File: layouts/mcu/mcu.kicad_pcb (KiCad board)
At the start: 2 copper layers, 15 parts

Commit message: Layouts: mcu: place and route mcu, add jlc design rules
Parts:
- C3, C4: value 100nF ±10% 50V X7R -> 20pF ±5% 50V C0G; footprint atopile:C0603-bd72f6 -> atopile:C0402-b3ef17
- R3: value 10kΩ ±1% 100mW -> 0Ω 100mW
- moved R5 26.6 mm to (6.60, -2.40)
- moved S2 17.5 mm to (-5.43, 9.60), turned to -90 degrees
- moved S1 16.6 mm to (4.17, 9.60), turned to 90 degrees
- moved C3 13.5 mm to (9.95, 2.65), turned to -90 degrees
- moved C2 13.1 mm to (-2.40, 8.30), turned to -90 degrees
- moved R2 12.1 mm to (1.60, 8.20), turned to -90 degrees
- moved R4 11.8 mm to (-0.75, 8.20), turned to -90 degrees
- moved R3 11.3 mm to (6.50, 3.20), turned to -90 degrees
- moved R6 9.29 mm to (-3.00, 11.2), turned to 90 degrees
- moved XTAL1 9.13 mm to (8.30, 3.80), turned to -90 degrees
- moved C4 7.90 mm to (9.95, 4.95), turned to 90 degrees
- moved C5 7.72 mm to (-1.42, 11.2), turned to -90 degrees
- moved R1 2.10 mm to (1.75, 11.2)
- moved C1 1.48 mm to (0.17, 11.2)
- turned U1 to 90 degrees
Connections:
- C1 pad 1: mcu.boot_switch.lp_filter-line -> mcu-line-5
- C1 pad 2: mcu.boot_switch.lp_filter-gnd -> gnd
- C2 pad 2: mcu-gnd -> gnd
- C3 pad 2: mcu-gnd -> gnd
- C4 pad 1: mcu-line-4 -> mcu-line-9
- C4 pad 2: mcu-gnd -> gnd
- C5 pad 1: mcu.reset_switch.lp_filter-line -> mcu-line-3
- C5 pad 2: mcu.reset_switch.lp_filter-gnd -> gnd
- R1 pad 2: mcu.boot_switch.lp_filter-line -> mcu-line-5
- R2 pad 1: mcu-line -> mcu-line-5
- R3 pad 2: mcu-line-1 -> mcu-line
- R4 pad 1: mcu-line-7 -> mcu-line-2
- R5 pad 1: mcu-line-9 -> mcu-line-4
- R6 pad 2: mcu.reset_switch.lp_filter-line -> mcu-line-3
- S1 pad 3: mcu-gnd -> gnd
- S1 pad 4: mcu-gnd -> gnd
- S2 pad 3: mcu-gnd -> gnd
- S2 pad 4: mcu-gnd -> gnd
- U1 pad 1: mcu-gnd -> gnd
- U1 pad 11: mcu-gnd -> gnd
- U1 pad 12: mcu-line-4 -> mcu-line-9
- U1 pad 13: mcu-line-1 -> mcu-line
- U1 pad 14: mcu-gnd -> gnd
- U1 pad 16: mcu.esp32_c3_mini_1.ic-line-5 -> mcu.esp32_c3_mini_1.ic-line-4
- U1 pad 18: mcu.esp32_c3_mini_1.ic-line-4 -> mcu.esp32_c3_mini_1.ic-line-5
- U1 pad 19: mcu.esp32_c3_mini_1.ic-line -> mcu.esp32_c3_mini_1.ic-line-3
- U1 pad 2: mcu-gnd -> gnd
- U1 pad 20: mcu.esp32_c3_mini_1.ic-line-3 -> mcu.esp32_c3_mini_1.ic-line-2
- U1 pad 21: mcu.esp32_c3_mini_1.ic-line-2 -> mcu.esp32_c3_mini_1.ic-line
- U1 pad 22: mcu-line-9 -> mcu-line-4
- U1 pad 23: mcu-line-8 -> mcu-line-3
- U1 pad 26: mcu-line-5 -> mcu-line-1
- U1 pad 27: mcu-line-3 -> mcu-line-6
- U1 pad 30: mcu-line-2 -> mcu-line-7
- U1 pad 31: mcu-line-6 -> mcu-line-8
- U1 pad 36: mcu-gnd -> gnd
- U1 pad 37: mcu-gnd -> gnd
- U1 pad 38: mcu-gnd -> gnd
- U1 pad 39: mcu-gnd -> gnd
- U1 pad 40: mcu-gnd -> gnd
- U1 pad 41: mcu-gnd -> gnd
- U1 pad 42: mcu-gnd -> gnd
- U1 pad 43: mcu-gnd -> gnd
- U1 pad 44: mcu-gnd -> gnd
- U1 pad 45: mcu-gnd -> gnd
- U1 pad 46: mcu-gnd -> gnd
- U1 pad 47: mcu-gnd -> gnd
- U1 pad 48: mcu-gnd -> gnd
- U1 pad 49: mcu-gnd -> gnd
- U1 pad 5: mcu-line-7 -> mcu-line-2
- U1 pad 50: mcu-gnd -> gnd
- U1 pad 51: mcu-gnd -> gnd
- U1 pad 52: mcu-gnd -> gnd
- U1 pad 53: mcu-gnd -> gnd
- U1 pad 54: mcu-gnd -> gnd
- U1 pad 55: mcu-gnd -> gnd
- U1 pad 56: mcu-gnd -> gnd
- U1 pad 57: mcu-gnd -> gnd
- U1 pad 58: mcu-gnd -> gnd
- U1 pad 59: mcu-gnd -> gnd
- U1 pad 60: mcu-gnd -> gnd
- U1 pad 61: mcu-gnd -> gnd
- U1 pad 8: mcu-line -> mcu-line-5
- XTAL1 pad 2: mcu-line-4 -> mcu-line-9
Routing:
- net mcu-line-3: track 0.00 -> 22.1 mm, vias 0 -> 2
- net mcu-gnd: track 10.9 -> 0.00 mm
- net hv: track 0.00 -> 7.66 mm, vias 0 -> 3
- net mcu-line-5: track 0.00 -> 7.37 mm
- net mcu.reset_switch-line: track 0.00 -> 5.64 mm
- net mcu.boot_switch-line: track 0.00 -> 5.63 mm
- net mcu-line-9: track 0.00 -> 5.28 mm
- net mcu.low_speed_crystal_clock-net: track 1.81 -> 3.66 mm
- net mcu-line: track 0.00 -> 1.57 mm
- net gnd: vias 0 -> 39
- added copper zone on F.Cu, net gnd

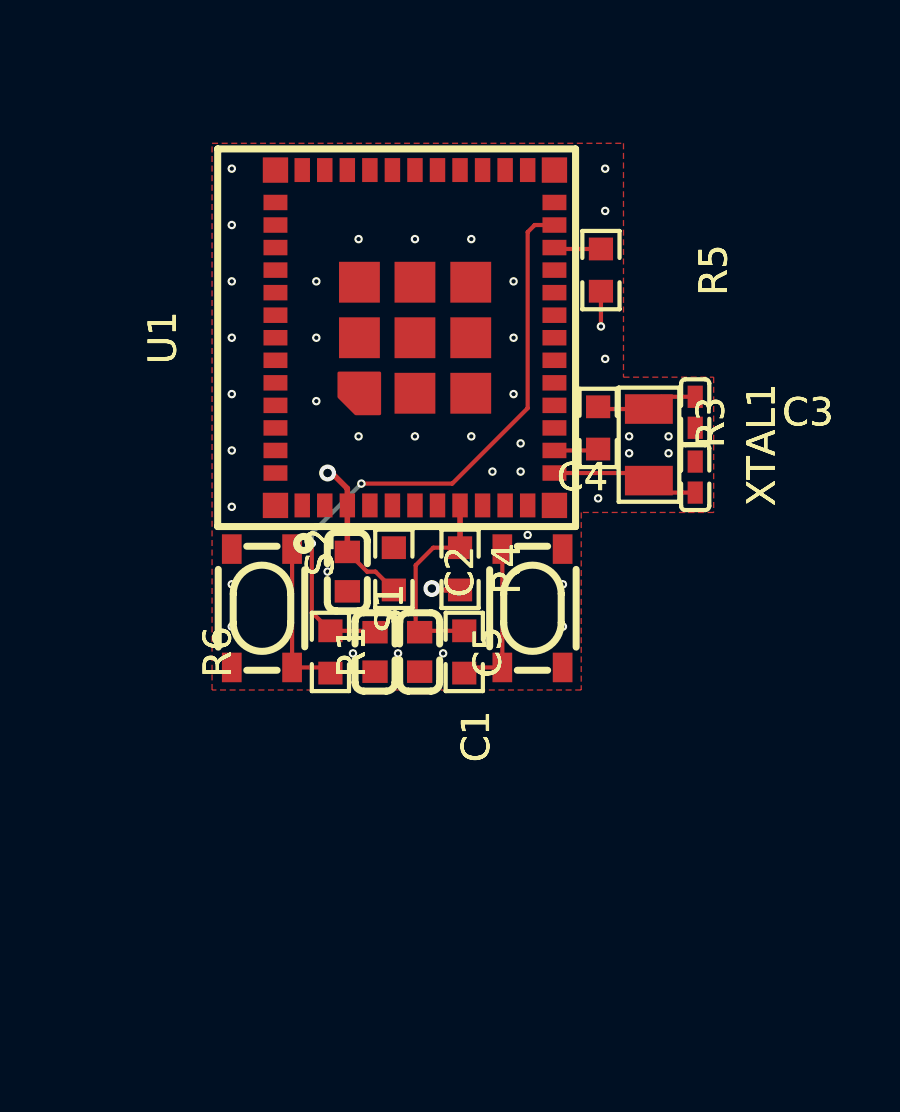
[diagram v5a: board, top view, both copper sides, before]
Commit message: Layouts: place light sensor between LEDs, add rule areas
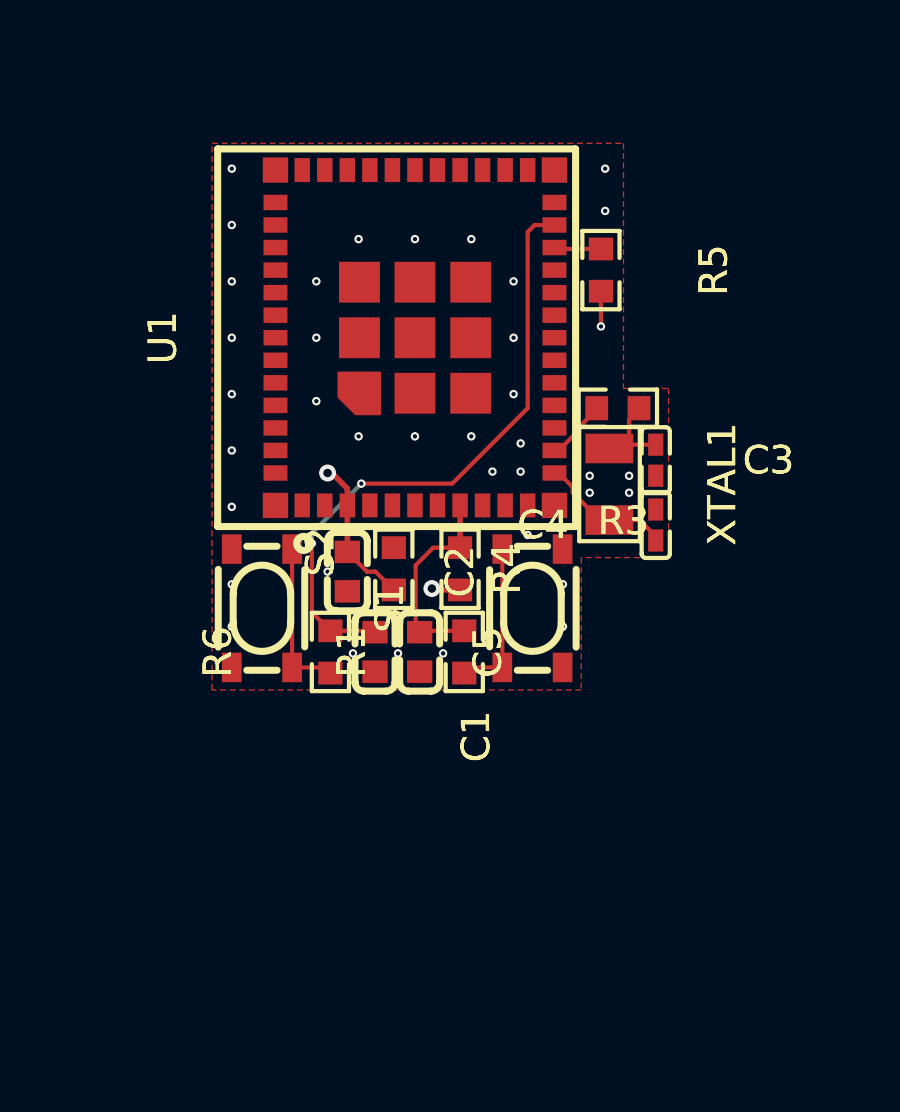
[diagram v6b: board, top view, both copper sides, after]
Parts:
- moved C3 2.20 mm to (8.54, 4.34)
- moved C4 2.20 mm to (8.54, 6.64)
- moved XTAL1 1.98 mm to (6.90, 5.20)
- moved R3 0.99 mm to (7.20, 2.50), turned to 180 degrees
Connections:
- C1 pad 1: mcu-line-5 -> mcu-line-1
- C4 pad 1: mcu-line-9 -> mcu-line
- C5 pad 1: mcu-line-3 -> mcu-line-6
- R1 pad 2: mcu-line-5 -> mcu-line-1
- R2 pad 1: mcu-line-5 -> mcu-line-1
- R3 pad 2: mcu-line -> mcu-line-4
- R5 pad 1: mcu-line-4 -> mcu-line-7
- R6 pad 2: mcu-line-3 -> mcu-line-6
- U1 pad 12: mcu-line-9 -> mcu-line
- U1 pad 13: mcu-line -> mcu-line-4
- U1 pad 16: mcu.esp32_c3_mini_1.ic-line-4 -> mcu.esp32_c3_mini_1.ic-line-2
- U1 pad 18: mcu.esp32_c3_mini_1.ic-line-5 -> mcu.esp32_c3_mini_1.ic-line-1
- U1 pad 19: mcu.esp32_c3_mini_1.ic-line-3 -> mcu.esp32_c3_mini_1.ic-line-5
- U1 pad 20: mcu.esp32_c3_mini_1.ic-line-2 -> mcu.esp32_c3_mini_1.ic-line-4
- U1 pad 22: mcu-line-4 -> mcu-line-7
- U1 pad 23: mcu-line-3 -> mcu-line-6
- U1 pad 26: mcu-line-1 -> mcu-line-8
- U1 pad 27: mcu-line-6 -> mcu-line-3
- U1 pad 30: mcu-line-7 -> mcu-line-9
- U1 pad 31: mcu-line-8 -> mcu-line-5
- U1 pad 6: mcu.esp32_c3_mini_1.ic-line-1 -> mcu.esp32_c3_mini_1.ic-line-3
- U1 pad 8: mcu-line-5 -> mcu-line-1
- XTAL1 pad 2: mcu-line-9 -> mcu-line
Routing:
- net mcu-line-6: track 0.00 -> 22.1 mm, vias 0 -> 2
- net mcu-line-3: track 22.1 -> 0.00 mm, vias 2 -> 0
- net mcu-line-5: track 7.37 -> 0.00 mm
- net mcu-line-1: track 0.00 -> 7.37 mm
- net mcu-line-9: track 5.28 -> 0.00 mm
- net mcu-line: track 1.57 -> 4.79 mm
- net mcu-line-7: track 0.00 -> 1.67 mm
- net mcu-line-4: track 1.67 -> 2.21 mm
- net gnd: vias 39 -> 37

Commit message: do some layouts
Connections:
- net mcu.low_speed_crystal_clock-net renamed unnamed[0]
- C1 pad 1: mcu-line-1 -> mcu-line
- C4 pad 1: mcu-line -> mcu-line-7
- C5 pad 1: mcu-line-6 -> mcu-line-2
- R1 pad 2: mcu-line-1 -> mcu-line
- R2 pad 1: mcu-line-1 -> mcu-line
- R4 pad 1: mcu-line-2 -> mcu-line-1
- R5 pad 1: mcu-line-7 -> mcu-line-9
- R6 pad 2: mcu-line-6 -> mcu-line-2
- U1 pad 12: mcu-line -> mcu-line-7
- U1 pad 16: mcu.esp32_c3_mini_1.ic-line-2 -> mcu.esp32_c3_mini_1.ic-line-3
- U1 pad 19: mcu.esp32_c3_mini_1.ic-line-5 -> mcu.esp32_c3_mini_1.ic-line-2
- U1 pad 21: mcu.esp32_c3_mini_1.ic-line -> mcu.esp32_c3_mini_1.ic-line-5
- U1 pad 22: mcu-line-7 -> mcu-line-9
- U1 pad 23: mcu-line-6 -> mcu-line-2
- U1 pad 26: mcu-line-8 -> mcu-line-5
- U1 pad 30: mcu-line-9 -> mcu-line-6
- U1 pad 31: mcu-line-5 -> mcu-line-8
- U1 pad 5: mcu-line-2 -> mcu-line-1
- U1 pad 6: mcu.esp32_c3_mini_1.ic-line-3 -> mcu.esp32_c3_mini_1.ic-line
- U1 pad 8: mcu-line-1 -> mcu-line
- XTAL1 pad 2: mcu-line -> mcu-line-7
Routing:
- net mcu-line-6: track 22.1 -> 0.00 mm, vias 2 -> 0
- net mcu-line-2: track 0.07 -> 22.1 mm, vias 0 -> 2
- net mcu-line-1: track 7.37 -> 0.07 mm
- net mcu-line-7: track 1.67 -> 4.79 mm
- net mcu-line: track 4.79 -> 7.37 mm
- net mcu-line-9: track 0.00 -> 1.67 mm
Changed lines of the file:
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@@
             (outputdirectory "")))
     (net 0 "")
-    (net 1 "mcu-line-8")
+    (net 1 "mcu-line-5")
     (net 2 "mcu.esp32_c3_mini_1.ic.footprint.pins[26].net-net")
-    (net 3 "mcu-line-9")
+    (net 3 "mcu-line-6")
     (net 4 "mcu.esp32_c3_mini_1.ic.footprint.pins[8].net-net")
     (net 5 "mcu.esp32_c3_mini_1.ic.footprint.pins[28].net-net")
-    (net 6 "mcu.esp32_c3_mini_1.ic-line-5")
+    (net 6 "mcu.esp32_c3_mini_1.ic-line-2")
     (net 7 "mcu.esp32_c3_mini_1.ic.footprint.pins[25].net-net")
-    (net 8 "mcu.esp32_c3_mini_1.ic-line-2")
+    (net 8 "mcu.esp32_c3_mini_1.ic-line-3")
     (net 9 "mcu-line-3")
     (net 10 "mcu.esp32_c3_mini_1.ic.footprint.pins[60].net-net")
-    (net 11 "mcu-line-7")
-    (net 12 "mcu.esp32_c3_mini_1.ic-line-3")
+    (net 11 "mcu-line-9")
+    (net 12 "mcu.esp32_c3_mini_1.ic-line")
     (net 13 "mcu.esp32_c3_mini_1.ic.footprint.pins[16].net-net")
-    (net 14 "mcu-line-2")
+    (net 14 "mcu-line-1")
     (net 15 "mcu.esp32_c3_mini_1.ic.footprint.pins[58].net-net")
     (net 16 "mcu.esp32_c3_mini_1.ic.footprint.pins[21].net-net")
     (net 17 "mcu.esp32_c3_mini_1.ic-line-1")
-    (net 18 "mcu.esp32_c3_mini_1.ic-line")
+    (net 18 "mcu.esp32_c3_mini_1.ic-line-5")
     (net 19 "hv")
-    (net 20 "mcu-line-5")
+    (net 20 "mcu-line-8")
     (net 21 "mcu.esp32_c3_mini_1.ic.footprint.pins[1].net-net")
     (net 22 "mcu-line-4")
@@
     (net 28 "mcu.esp32_c3_mini_1.ic.footprint.pins[17].net-net")
     (net 29 "mcu.esp32_c3_mini_1.ic.footprint.pins[27].net-net")
-    (net 30 "mcu-line")
+    (net 30 "mcu-line-7")
     (net 31 "mcu.boot_switch-line")
     (net 32 "mcu.reset_switch-line")
-    (net 33 "mcu.low_speed_crystal_clock-net")
-    (net 34 "mcu-line-1")
-    (net 35 "mcu-line-6")
+    (net 33 "unnamed[0]")
+    (net 34 "mcu-line")
+    (net 35 "mcu-line-2")
     (footprint "atopile:KEY-SMD_4P-L4.2-W3.2-P2.20-LS4.6-a2ccf0"
         (layer "F.Cu")
@@
             (layers "F.Cu" "F.Paste" "F.Mask")
             (remove_unused_layers no)
-            (net 35 "mcu-line-6")))
+            (net 35 "mcu-line-2")))
     (footprint "atopile:C0603-bd72f6"
         (layer "F.Cu")
@@
             (layers "F.Cu" "F.Paste" "F.Mask")
             (remove_unused_layers no)
-            (net 34 "mcu-line-1"))
+            (net 34 "mcu-line"))
         (pad "2" smd rect
             (at 0.7 0 270)
@@
             (layers "F.Cu" "F.Paste" "F.Mask")
             (remove_unused_layers no)
-            (net 33 "mcu.low_speed_crystal_clock-net"))
+            (net 33 "unnamed[0]"))
         (pad "2" smd rect
             (at 0.55 0 270)
@@
             (layers "F.Cu" "F.Paste" "F.Mask")
             (remove_unused_layers no)
-            (net 35 "mcu-line-6"))
+            (net 35 "mcu-line-2"))
         (pad "2" smd rect
             (at 0.7 0 270)
@@
             (layers "F.Cu" "F.Paste" "F.Mask")
             (remove_unused_layers no)
-            (net 14 "mcu-line-2"))
+            (net 14 "mcu-line-1"))
         (pad "2" smd rect
             (at 0.75 0 270)
@@
             (layers "F.Cu" "F.Paste" "F.Mask")
             (remove_unused_layers no)
-            (net 34 "mcu-line-1"))
+            (net 34 "mcu-line"))
         (pad "2" smd rect
             (at 0.75 0 270)
@@
             (layers "F.Cu" "F.Paste" "F.Mask")
             (remove_unused_layers no)
-            (net 30 "mcu-line"))
+            (net 30 "mcu-line-7"))
         (pad "2" smd rect
             (at 0.55 0 90)
@@
             (layers "F.Cu" "F.Paste" "F.Mask")
             (remove_unused_layers no)
-            (net 33 "mcu.low_speed_crystal_clock-net"))
+            (net 33 "unnamed[0]"))
         (pad "2" smd rect
             (at 1.27 0 270)
@@
             (layers "F.Cu" "F.Paste" "F.Mask")
             (remove_unused_layers no)
-            (net 30 "mcu-line")))
+            (net 30 "mcu-line-7")))
     (footprint "atopile:WIFIM-SMD_ESP32-C3-MINI-MINI-1U-1cb675"
         (layer "F.Cu")
@@
             (layers "F.Cu" "F.Paste" "F.Mask")
             (remove_unused_layers no)
-            (net 14 "mcu-line-2"))
+            (net 14 "mcu-line-1"))
         (pad "6" smd rect
             (at -5.95 0 90)
@@
             (layers "F.Cu" "F.Paste" "F.Mask")
             (remove_unused_layers no)
-            (net 12 "mcu.esp32_c3_mini_1.ic-line-3"))
+            (net 12 "mcu.esp32_c3_mini_1.ic-line"))
         (pad "7" smd rect
             (at -5.95 0.8 90)
@@
             (layers "F.Cu" "F.Paste" "F.Mask")
             (remove_unused_layers no)
-            (net 34 "mcu-line-1"))
+            (net 34 "mcu-line"))
         (pad "9" smd rect
             (at -5.95 2.4 90)
@@
             (layers "F.Cu" "F.Paste" "F.Mask")
             (remove_unused_layers no)
-            (net 30 "mcu-line"))
+            (net 30 "mcu-line-7"))
         (pad "13" smd rect
             (at -4 4.95 180)
@@
             (layers "F.Cu" "F.Paste" "F.Mask")
             (remove_unused_layers no)
-            (net 8 "mcu.esp32_c3_mini_1.ic-line-2"))
+            (net 8 "mcu.esp32_c3_mini_1.ic-line-3"))
         (pad "17" smd rect
             (at -0.8 4.95 180)
@@
             (layers "F.Cu" "F.Paste" "F.Mask")
             (remove_unused_layers no)
-            (net 6 "mcu.esp32_c3_mini_1.ic-line-5"))
+            (net 6 "mcu.esp32_c3_mini_1.ic-line-2"))
         (pad "20" smd rect
             (at 1.6 4.95 180)
@@
             (layers "F.Cu" "F.Paste" "F.Mask")
             (remove_unused_layers no)
-            (net 18 "mcu.esp32_c3_mini_1.ic-line"))
+            (net 18 "mcu.esp32_c3_mini_1.ic-line-5"))
         (pad "22" smd rect
             (at 3.2 4.95 180)
@@
             (layers "F.Cu" "F.Paste" "F.Mask")
             (remove_unused_layers no)
-            (net 11 "mcu-line-7"))
+            (net 11 "mcu-line-9"))
         (pad "23" smd rect
             (at 4 4.95 180)
@@
             (layers "F.Cu" "F.Paste" "F.Mask")
             (remove_unused_layers no)
-            (net 35 "mcu-line-6"))
+            (net 35 "mcu-line-2"))
         (pad "24" smd rect
             (at 4.8 4.95 180)
@@
             (layers "F.Cu" "F.Paste" "F.Mask")
             (remove_unused_layers no)
-            (net 1 "mcu-line-8"))
+            (net 1 "mcu-line-5"))
         (pad "27" smd rect
             (at 5.95 2.4 270)
@@
             (layers "F.Cu" "F.Paste" "F.Mask")
             (remove_unused_layers no)
-            (net 3 "mcu-line-9"))
+            (net 3 "mcu-line-6"))
         (pad "31" smd rect
             (at 5.95 -0.8 90)
@@
             (layers "F.Cu" "F.Paste" "F.Mask")
             (remove_unused_layers no)
-            (net 20 "mcu-line-5"))
+            (net 20 "mcu-line-8"))
         (pad "32" smd rect
             (at 5.95 -1.6 90)
@@
             (layers "F.Cu" "F.Paste" "F.Mask")
             (remove_unused_layers no)
-            (net 11 "mcu-line-7"))
+            (net 11 "mcu-line-9"))
         (pad "2" smd rect
             (at 0.75 0 270)
@@
             (layers "F.Cu" "F.Paste" "F.Mask")
             (remove_unused_layers no)
-            (net 34 "mcu-line-1")))
+            (net 34 "mcu-line")))
     (footprint "atopile:R0603-ebcab9"
         (layer "F.Cu")
@@
             (layers "F.Cu" "F.Paste" "F.Mask")
             (remove_unused_layers no)
-            (net 33 "mcu.low_speed_crystal_clock-net"))
+            (net 33 "unnamed[0]"))
         (pad "2" smd rect
             (at 0.75 0 180)

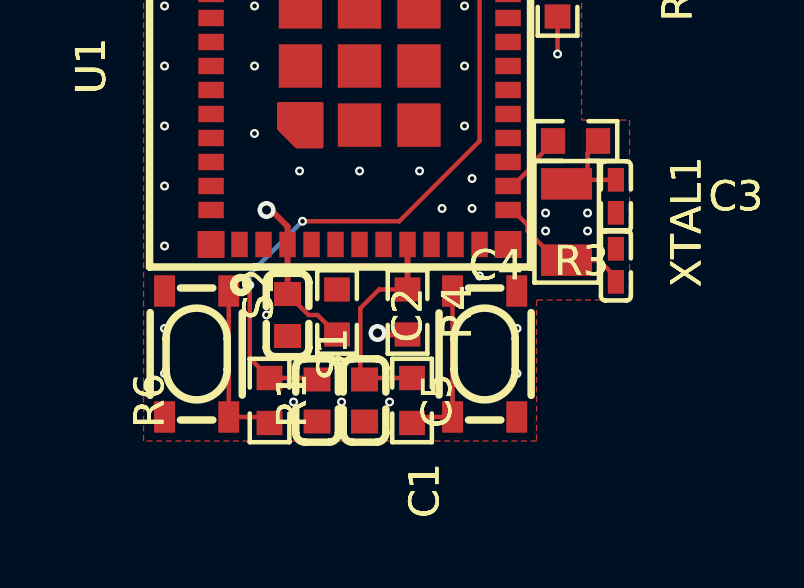
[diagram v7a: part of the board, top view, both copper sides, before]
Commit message: Try to fix fuses
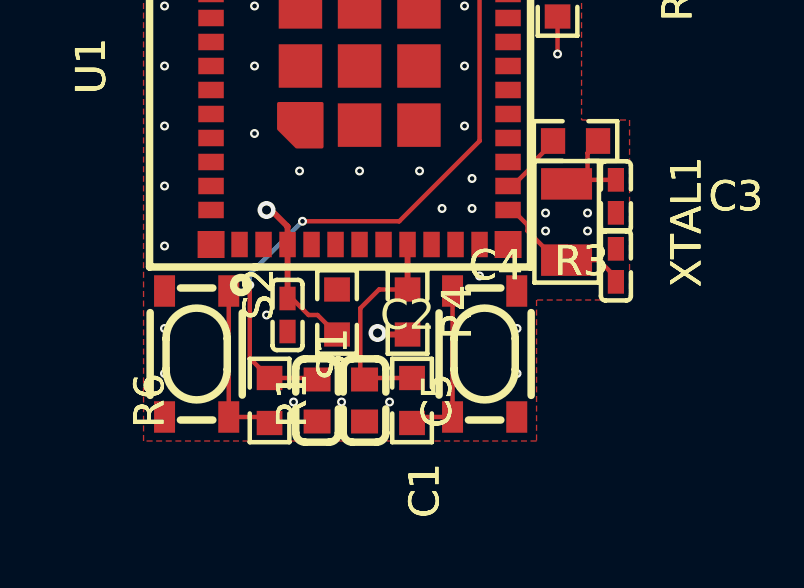
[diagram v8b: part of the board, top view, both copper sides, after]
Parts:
- C2: value 1µF ±10% 50V X5R -> 1µF ±10% 25V X5R; footprint atopile:C0603-bd72f6 -> atopile:C0402-b3ef17
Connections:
- net unnamed[0] renamed mcu.low_speed_crystal_clock-net
- C4 pad 1: mcu-line-7 -> mcu-line-1
- C5 pad 1: mcu-line-2 -> mcu-line-7
- R4 pad 1: mcu-line-1 -> mcu-line-5
- R6 pad 2: mcu-line-2 -> mcu-line-7
- U1 pad 12: mcu-line-7 -> mcu-line-1
- U1 pad 16: mcu.esp32_c3_mini_1.ic-line-3 -> mcu.esp32_c3_mini_1.ic-line-1
- U1 pad 18: mcu.esp32_c3_mini_1.ic-line-1 -> mcu.esp32_c3_mini_1.ic-line
- U1 pad 19: mcu.esp32_c3_mini_1.ic-line-2 -> mcu.esp32_c3_mini_1.ic-line-4
- U1 pad 20: mcu.esp32_c3_mini_1.ic-line-4 -> mcu.esp32_c3_mini_1.ic-line-2
- U1 pad 21: mcu.esp32_c3_mini_1.ic-line-5 -> mcu.esp32_c3_mini_1.ic-line-3
- U1 pad 23: mcu-line-2 -> mcu-line-7
- U1 pad 26: mcu-line-5 -> mcu-line-6
- U1 pad 27: mcu-line-3 -> mcu-line-2
- U1 pad 30: mcu-line-6 -> mcu-line-3
- U1 pad 5: mcu-line-1 -> mcu-line-5
- U1 pad 6: mcu.esp32_c3_mini_1.ic-line -> mcu.esp32_c3_mini_1.ic-line-5
- XTAL1 pad 2: mcu-line-7 -> mcu-line-1
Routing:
- net mcu-line-2: track 22.1 -> 0.00 mm, vias 2 -> 0
- net mcu-line-7: track 4.79 -> 22.1 mm, vias 0 -> 2
- net mcu-line-1: track 0.07 -> 4.79 mm
